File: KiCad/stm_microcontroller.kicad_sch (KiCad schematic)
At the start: 22 parts, among them J4 Conn_ARM_SWD_TagConnect_TC203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, J5 USB_C_Receptacle_USB2.0_14P, SW1 SW_Push, SW2 SW_Push, U1 STM32F103C8Tx, Y1 8Mhz

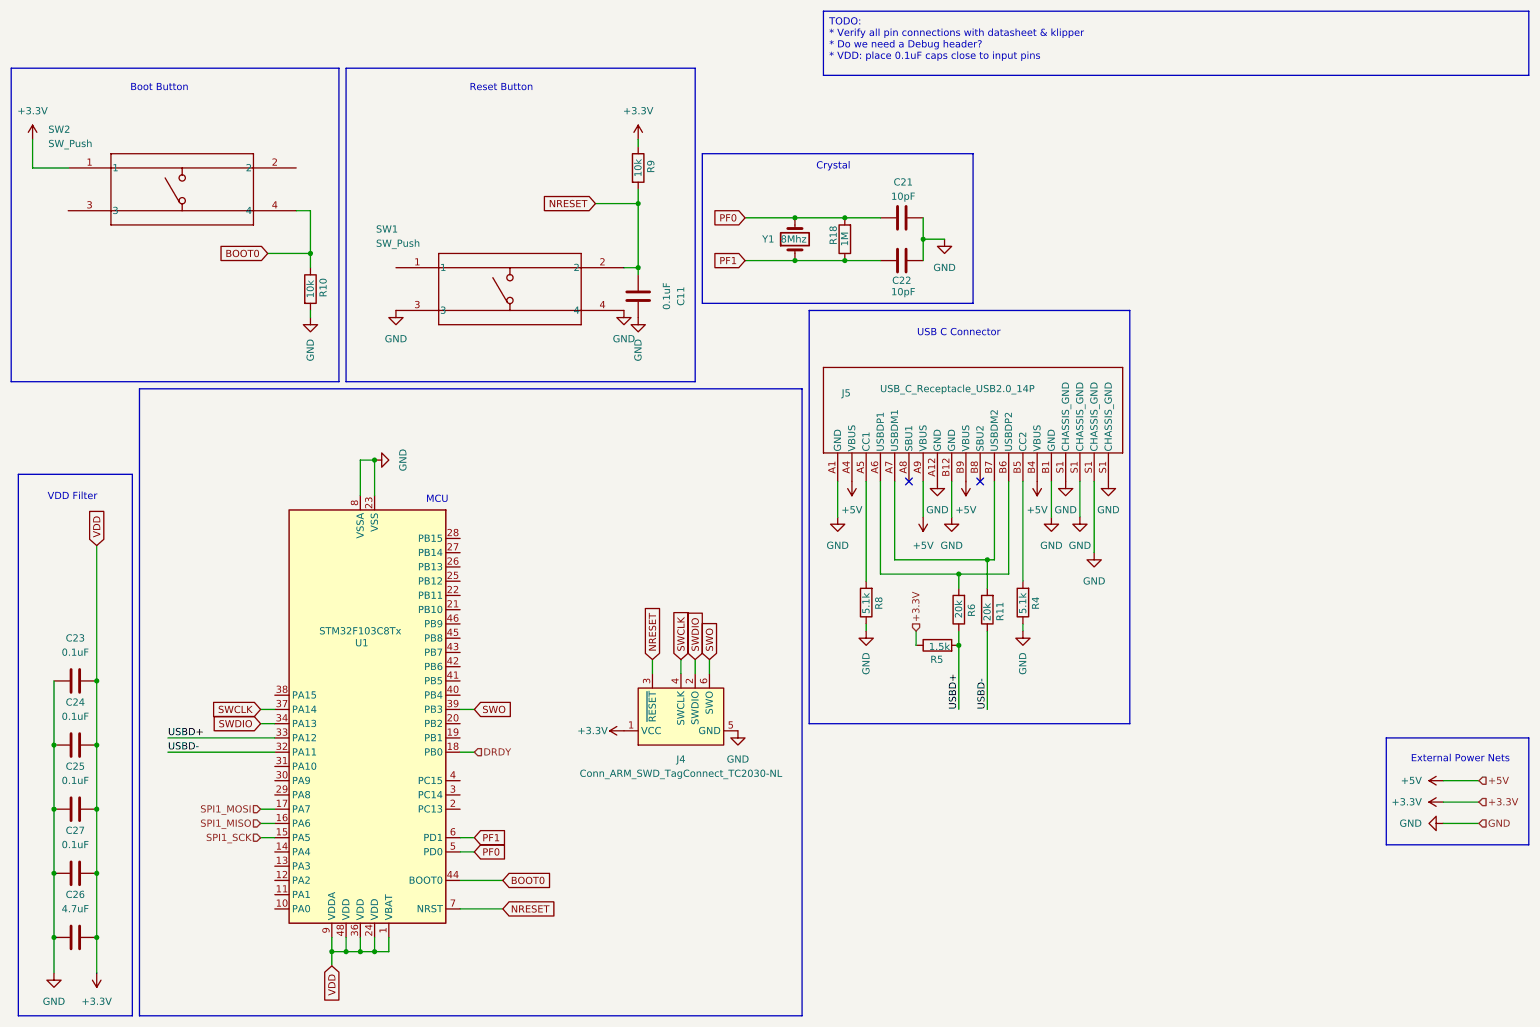
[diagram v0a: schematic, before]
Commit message: Crystal Changes
* Update crystal selection, schematic and footprint
* Add resistor to limit drive current to crystal
* Block ground plane fill under crystal circuit
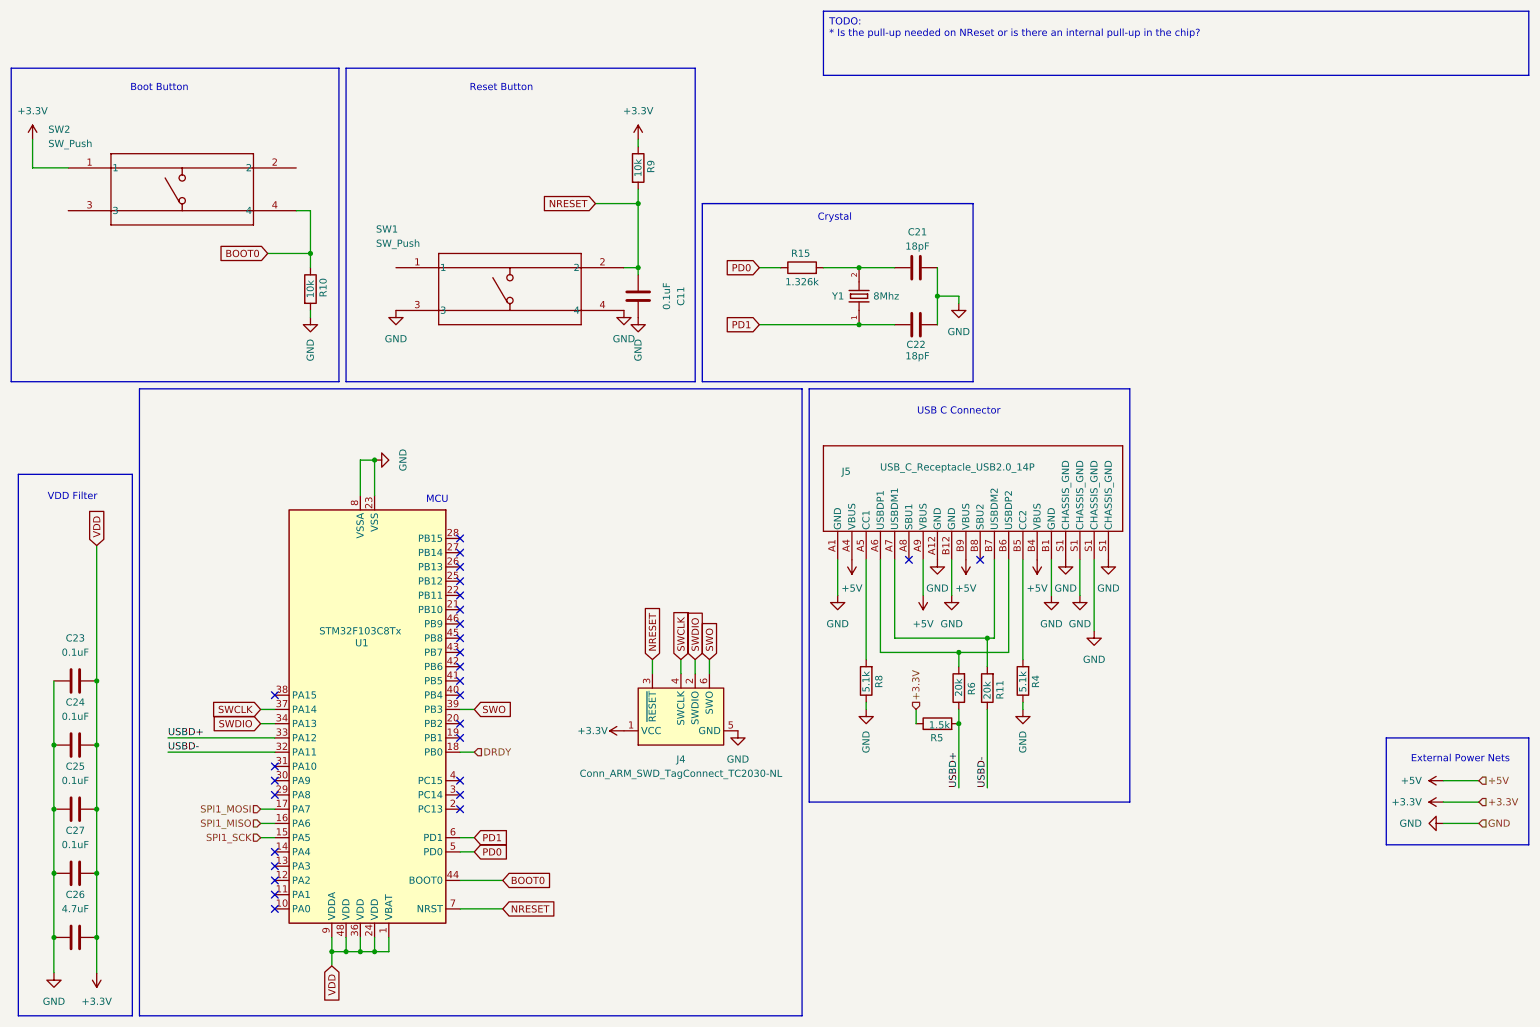
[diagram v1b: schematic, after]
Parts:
- removed R18: 1M, Resistor_SMD:R_0805_2012Metric_Pad1.20x1.40mm_HandSolder, symbol Device:R
- added R15: 1.326k, Resistor_SMD:R_0805_2012Metric_Pad1.20x1.40mm_HandSolder, symbol Device:R
- C21, C22: value 10pF -> 18pF
- J5: footprint CONN16_USB4085-GF-A_GCT -> Connector_USB:USB_C_Receptacle_GCT_USB4085
- Y1: footprint Crystal:Crystal_SMD_Abracon_ABM3-2Pin_5.0x3.2mm -> Library:XTAL_ECS-80-18-30-JGN-TR; symbol Device:Crystal -> ECS_80_18_30_JGN_TR:ECS-80-18-30-JGN-TR; AVAILABILITY (none) -> Good; MANUFACTURER (none) -> ECS INC; MP (none) -> ECX-53; PACKAGE (none) -> SMD-2 ECX; PARTREV (none) -> 2017; STANDARD (none) -> Manufacturer Recommendation
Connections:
- net PF0: no longer names the net of C21.1, Y1.2
- net PF0: now also R15.2; no longer U1.5 (PD0)
- net PF1 renamed PD1
- new net PD0: R15.1, U1.5 (PD0)
- no-connect marks 2 -> 28
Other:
- moved on the sheet: C21, C22, J5, R11, R4, R5, R6, R8

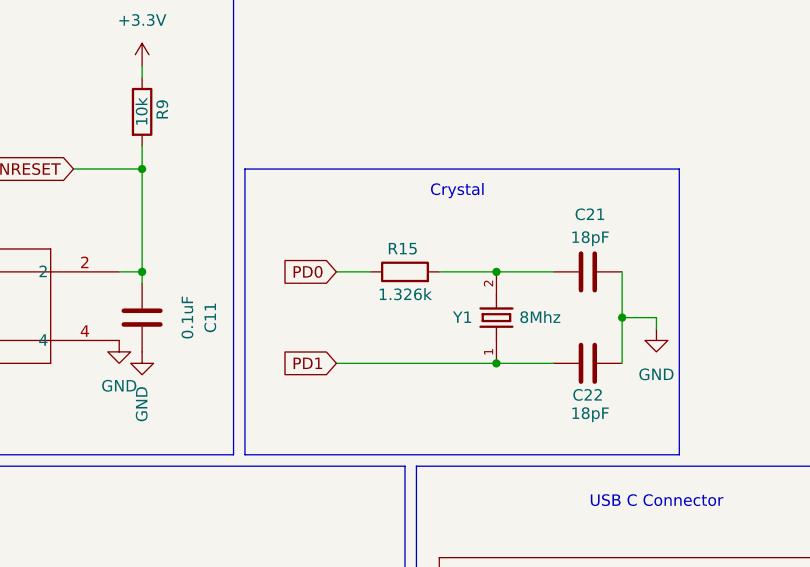
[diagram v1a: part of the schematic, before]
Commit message: Update Rext value
1.1k is an approximate value for the resistance required.
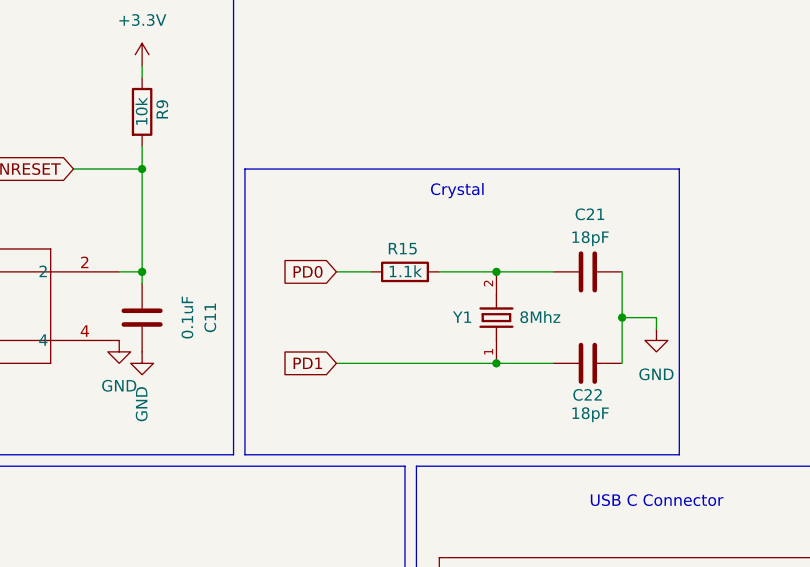
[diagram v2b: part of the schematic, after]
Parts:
- R15: value 1.326k -> 1.1k
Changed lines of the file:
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@@
 			)
 		)
-		(property "Value" "1.326k"
-			(at 153.67 62.23 90)
+		(property "Value" "1.1k"
+			(at 153.67 59.69 90)
 			(effects
 				(font

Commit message: Work In Progress
moving towards v 2
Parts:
- removed J4: Conn_ARM_SWD_TagConnect_TC2030-NL, Connector:Tag-Connect_TC2030-IDC-NL_2x03_P1.27mm_Vertical, symbol Connector:Conn_ARM_SWD_TagConnect_TC2030-NL
- removed SW1, SW2: SW_Push, SWITCH_43SMTR92LFS, symbol PTS645 Switch:PTS645SM43SMTR92LFS
- added D4: LED, LED_SMD:LED_1206_3216Metric_Pad1.42x1.75mm_HandSolder, symbol Device:LED
- added J6, J8: Conn_01x02, Connector_PinHeader_2.54mm:PinHeader_1x02_P2.54mm_Vertical, symbol Connector_Generic:Conn_01x02
- added SWD_Header1: Conn_02x03_Counter_Clockwise, Connector_PinHeader_2.54mm:PinHeader_2x03_P2.54mm_Vertical, symbol Connector_Generic:Conn_02x03_Counter_Clockwise
- C21, C22: value 18pF -> 30pF
- R15: value 1.1k -> 620R
- U1: footprint Package_QFP:LQFP-48_7x7mm_P0.5mm -> STM32F103C8T6TR:LQFP48_STM
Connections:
- net +3.3V: now also J8.1 (Pin_1), SWD_Header1.1 (Pin_1), SWD_Header1.2 (Pin_2)
- net BOOT0: now also J8.2 (Pin_2)
- net GND: now also D4.1 (K), J6.1 (Pin_1), SWD_Header1.5 (Pin_5), SWD_Header1.6 (Pin_6); no longer J5.S1 (CHASSIS_GND)
- net NRESET: now also J6.2 (Pin_2)
- net PD0: now also C21.1, Y1.2; no longer R15.1
- net SWCLK: now also SWD_Header1.4 (Pin_4)
- net SWDIO: now also SWD_Header1.3 (Pin_3)
- net at U1.25 (PB12): now also R15.2
- net SWO: no longer names the net of U1.39 (PB3)
- new net: D4.2 (A), R15.1
- new net Earth: J5.S1 (CHASSIS_GND)
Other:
- note added: "Boot0 Header"
- note added: "Reset Header"
- note removed: "Boot Button"
- note removed: "Reset Button"
- moved on the sheet: C11, R10, R9
